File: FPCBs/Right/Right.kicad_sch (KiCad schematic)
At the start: 23 parts, among them J1 PCB, J4 shutter+1st_dial, J5 2nd Focus+Shutter, J6 FPC Focus/Shutter, SW1 Mode Dial, SW2 ON/OFF, SW3 Focus+Shutter 1, SW4 Focus+Shutter 2, U1 SG-105, U2 SG-105

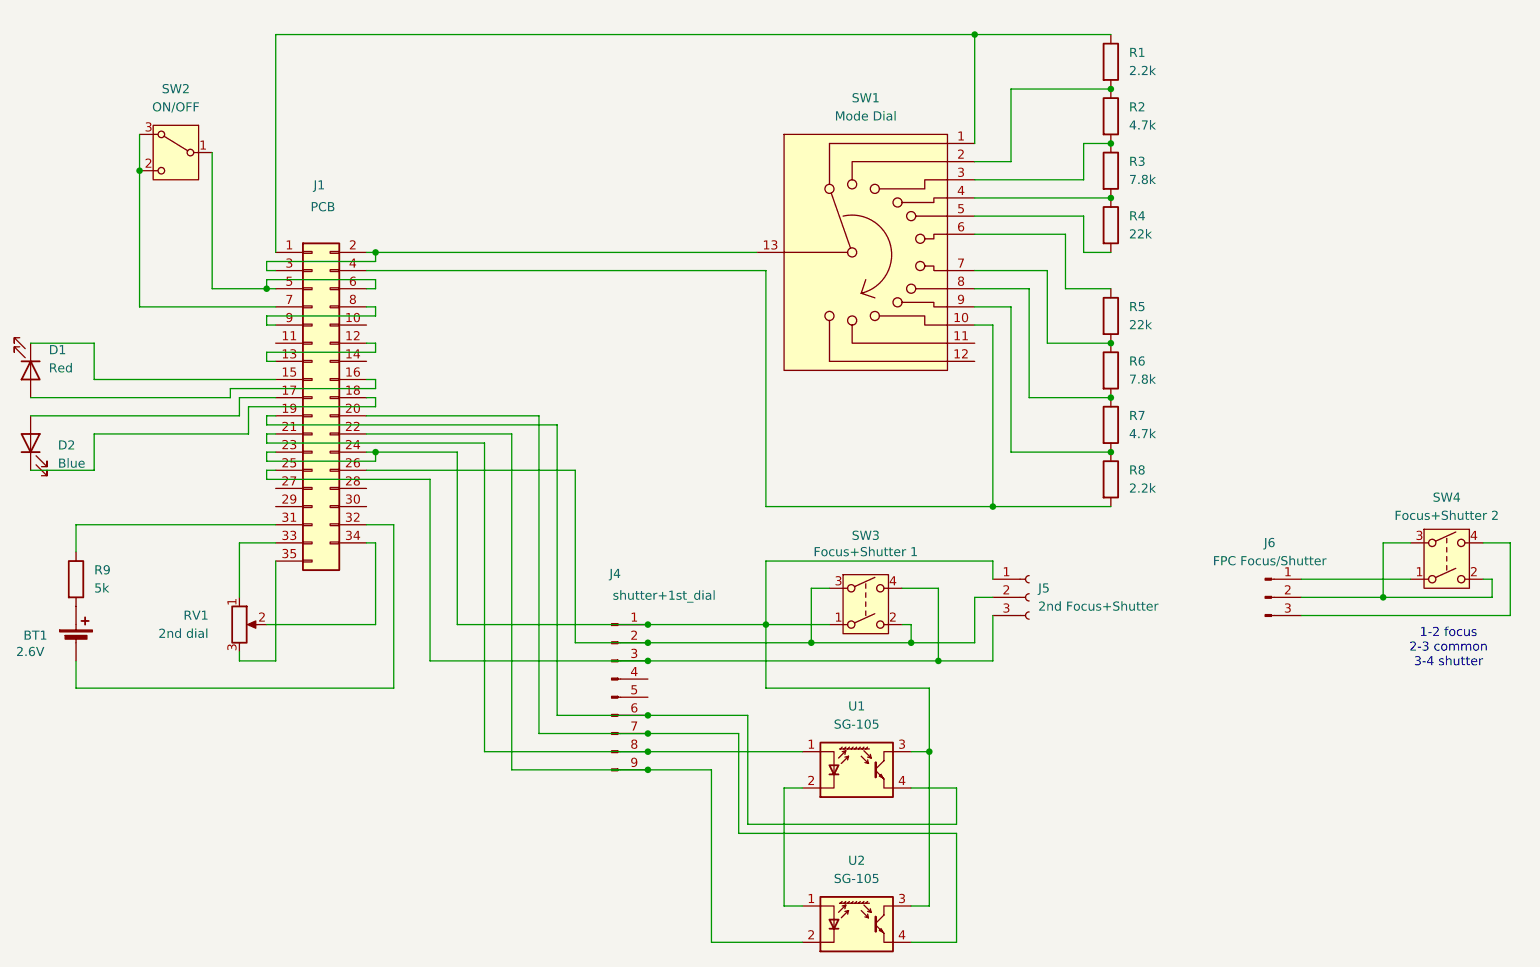
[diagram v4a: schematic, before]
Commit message: Add 1st dial connector
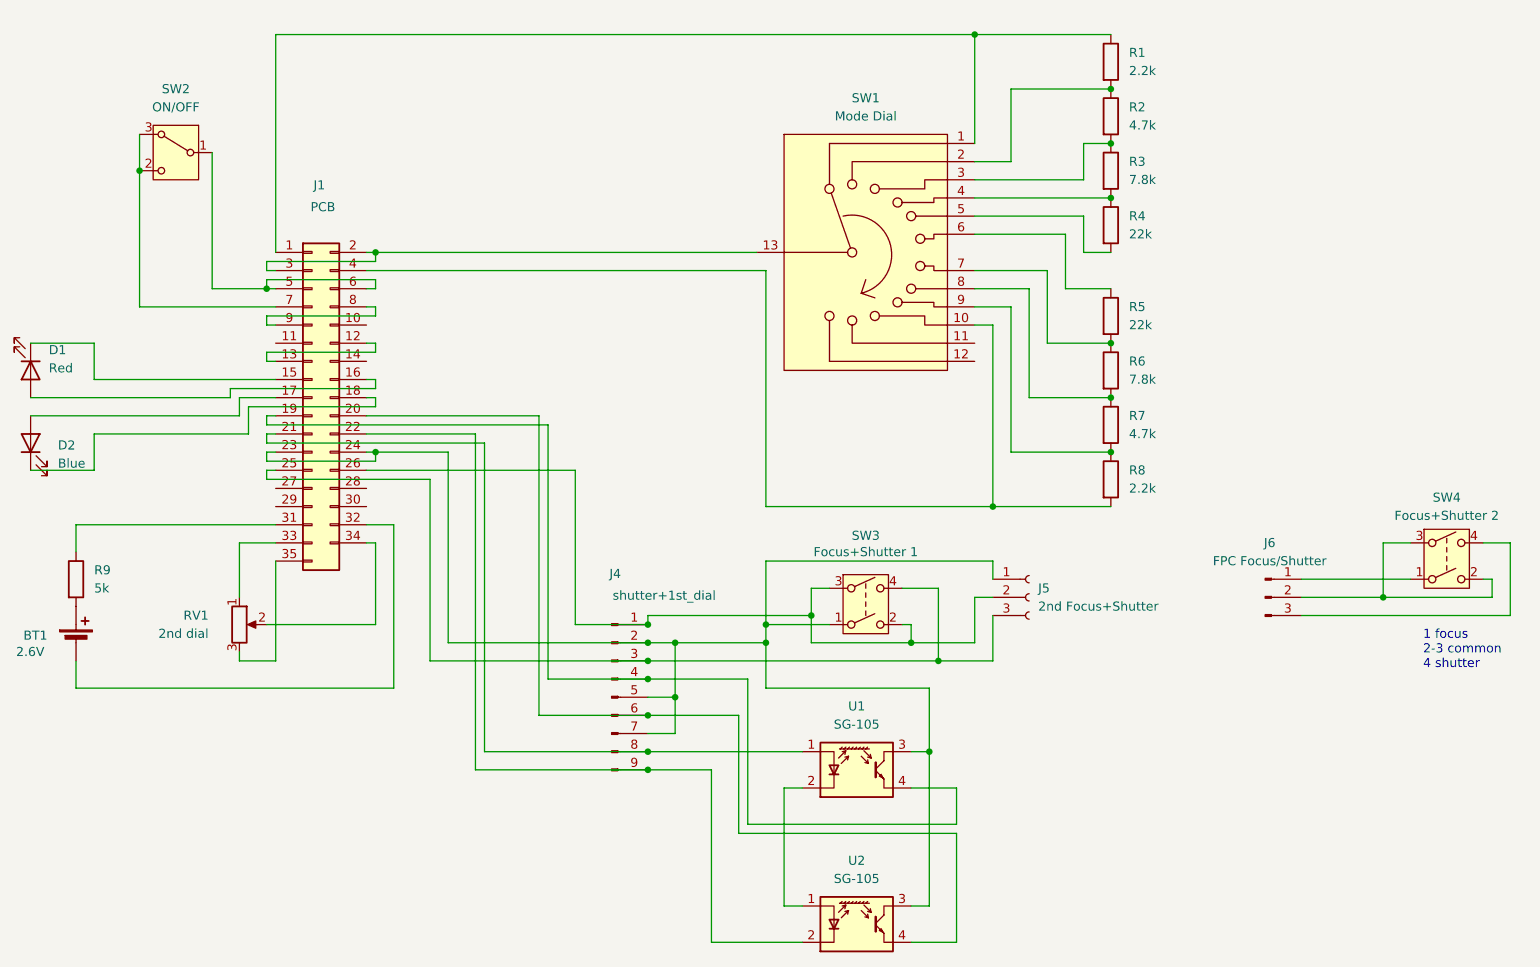
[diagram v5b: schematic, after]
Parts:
- J4: footprint (none) -> Leica-G9ii:Connector-2Rows-9Pins-0.60mm
- R1, R2, R3, R4, R5, R6, R7, R8: footprint Leica-G9ii:R_2x1mm -> Leica-G9ii:R_0603
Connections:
- net at J1.19 (Pin_19), U1.4 (E): now also J4.4 (Pin_4); no longer J4.6 (Pin_6)
- net at J1.20 (Pin_20), U2.4 (E): now also J4.6 (Pin_6); no longer J4.7 (Pin_7)
- net at J1.23 (Pin_23), J1.24 (Pin_24), J5.1 (Pin_1)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: now also J4.2 (Pin_2), J4.5 (Pin_5), J4.7 (Pin_7); no longer J4.1 (Pin_1)
- net at J1.26 (Pin_26), J5.2 (Pin_2), SW3.2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: now also J4.1 (Pin_1); no longer J4.2 (Pin_2)
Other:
- note added: "1 focus 2-3 common 4 shutter"
- note removed: "1-2 focus 2-3 common 3-4 shutter"
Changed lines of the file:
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@@
 	(generator_version "9.0")
 	(paper "A4")
-	(text "1-2 focus\n2-3 common\n3-4 shutter"
+	(text "1 focus\n2-3 common\n4 shutter"
 		(exclude_from_sim no)
-		(at 244.094 112.522 0)
+		(at 240.538 112.776 0)
 		(effects
 			(font
 				(size 1.27 1.27)
 			)
+			(justify left)
 		)
 	)
@@
 	)
 	(junction
-		(at 132.08 111.76)
-		(diameter 0)
-		(color 0 0 0 0)
-	)
-	(junction
 		(at 196.85 69.85)
 		(diameter 0)
@@
 	)
 	(junction
+		(at 132.08 109.22)
+		(diameter 0)
+		(color 0 0 0 0)
+	)
+	(junction
 		(at 60.96 45.72)
 		(diameter 0)
@@
 	)
 	(junction
-		(at 196.85 77.47)
+		(at 135.89 119.38)
 		(diameter 0)
 		(color 0 0 0 0)
 	)
 	(junction
-		(at 132.08 127)
+		(at 196.85 77.47)
 		(diameter 0)
 		(color 0 0 0 0)
 	)
 	(junction
-		(at 132.08 109.22)
+		(at 132.08 127)
 		(diameter 0)
 		(color 0 0 0 0)
@@
 	)
 	(junction
-		(at 148.59 109.22)
+		(at 180.34 92.71)
 		(diameter 0)
 		(color 0 0 0 0)
 	)
 	(junction
-		(at 180.34 92.71)
+		(at 154.94 107.95)
 		(diameter 0)
 		(color 0 0 0 0)
 	)
 	(junction
-		(at 132.08 121.92)
+		(at 148.59 109.22)
 		(diameter 0)
 		(color 0 0 0 0)
 	)
 	(junction
-		(at 154.94 111.76)
+		(at 132.08 111.76)
 		(diameter 0)
 		(color 0 0 0 0)
@@
 	)
 	(junction
+		(at 132.08 116.84)
+		(diameter 0)
+		(color 0 0 0 0)
+	)
+	(junction
+		(at 135.89 111.76)
+		(diameter 0)
+		(color 0 0 0 0)
+	)
+	(junction
 		(at 172.72 114.3)
 		(diameter 0)
@@
 	)
 	(junction
-		(at 132.08 124.46)
+		(at 148.59 111.76)
 		(diameter 0)
 		(color 0 0 0 0)
@@
 		(color 0 0 0 0)
 	)
+	(junction
+		(at 132.08 121.92)
+		(diameter 0)
+		(color 0 0 0 0)
+	)
 	(wire
 		(pts
@@
 	(wire
 		(pts
+			(xy 132.08 107.95) (xy 132.08 109.22)
+		)
+		(stroke
+			(width 0)
+			(type default)
+		)
+	)
+	(wire
+		(pts
 			(xy 78.74 72.39) (xy 80.01 72.39)
 		)
@@
 	(wire
 		(pts
-			(xy 146.05 137.16) (xy 146.05 121.92)
+			(xy 146.05 137.16) (xy 146.05 116.84)
 		)
 		(stroke
@@
 	(wire
 		(pts
-			(xy 105.41 85.09) (xy 105.41 109.22)
+			(xy 104.14 85.09) (xy 104.14 111.76)
 		)
 		(stroke
@@
 	(wire
 		(pts
-			(xy 119.38 121.92) (xy 132.08 121.92)
+			(xy 118.11 116.84) (xy 132.08 116.84)
 		)
 		(stroke
@@
 	(wire
 		(pts
-			(xy 92.71 82.55) (xy 113.03 82.55)
+			(xy 92.71 82.55) (xy 107.95 82.55)
 		)
 		(stroke
@@
 	(wire
 		(pts
-			(xy 132.08 121.92) (xy 146.05 121.92)
+			(xy 132.08 116.84) (xy 146.05 116.84)
 		)
 		(stroke
@@
 	(wire
 		(pts
-			(xy 121.92 87.63) (xy 121.92 111.76)
+			(xy 121.92 87.63) (xy 121.92 109.22)
 		)
 		(stroke
@@
 	(wire
 		(pts
-			(xy 105.41 109.22) (xy 132.08 109.22)
+			(xy 135.89 124.46) (xy 132.08 124.46)
+		)
+		(stroke
+			(width 0)
+			(type default)
+		)
+	)
+	(wire
+		(pts
+			(xy 104.14 111.76) (xy 132.08 111.76)
 		)
 		(stroke
@@
 	(wire
 		(pts
-			(xy 113.03 82.55) (xy 113.03 129.54)
+			(xy 107.95 82.55) (xy 107.95 129.54)
 		)
 		(stroke
@@
 	(wire
 		(pts
+			(xy 148.59 100.33) (xy 148.59 109.22)
+		)
+		(stroke
+			(width 0)
+			(type default)
+		)
+	)
+	(wire
+		(pts
 			(xy 177.8 54.61) (xy 190.5 54.61)
 		)
@@
 	(wire
 		(pts
-			(xy 148.59 118.11) (xy 148.59 109.22)
+			(xy 148.59 118.11) (xy 148.59 111.76)
 		)
 		(stroke
@@
 	(wire
 		(pts
-			(xy 116.84 124.46) (xy 132.08 124.46)
+			(xy 154.94 104.14) (xy 154.94 107.95)
+		)
+		(stroke
+			(width 0)
+			(type default)
+		)
+	)
+	(wire
+		(pts
+			(xy 116.84 121.92) (xy 132.08 121.92)
 		)
 		(stroke
@@
 	(wire
 		(pts
+			(xy 135.89 111.76) (xy 135.89 119.38)
+		)
+		(stroke
+			(width 0)
+			(type default)
+		)
+	)
+	(wire
+		(pts
 			(xy 171.45 127) (xy 171.45 148.59)
 		)
@@
 	(wire
 		(pts
-			(xy 93.98 109.22) (xy 93.98 97.79)
+			(xy 148.59 109.22) (xy 148.59 111.76)
 		)
 		(stroke
@@
 	(wire
 		(pts
-			(xy 154.94 104.14) (xy 154.94 111.76)
+			(xy 93.98 109.22) (xy 93.98 97.79)
 		)
 		(stroke
@@
 	(wire
 		(pts
-			(xy 78.74 81.28) (xy 119.38 81.28)
+			(xy 78.74 81.28) (xy 118.11 81.28)
 		)
 		(stroke
@@
 	(wire
 		(pts
-			(xy 121.92 111.76) (xy 132.08 111.76)
-		)
-		(stroke
-			(width 0)
-			(type default)
-		)
-	)
-	(wire
-		(pts
 			(xy 74.93 105.41) (xy 74.93 97.79)
 		)
@@
 	(wire
 		(pts
-			(xy 93.98 85.09) (xy 105.41 85.09)
+			(xy 93.98 85.09) (xy 104.14 85.09)
 		)
 		(stroke
@@
 	(wire
 		(pts
-			(xy 132.08 109.22) (xy 148.59 109.22)
+			(xy 132.08 111.76) (xy 135.89 111.76)
 		)
 		(stroke
@@
 	(wire
 		(pts
-			(xy 132.08 111.76) (xy 154.94 111.76)
+			(xy 121.92 109.22) (xy 132.08 109.22)
 		)
 		(stroke
@@
 	(wire
 		(pts
-			(xy 116.84 80.01) (xy 116.84 124.46)
+			(xy 116.84 80.01) (xy 116.84 121.92)
 		)
 		(stroke
@@
 	(wire
 		(pts
-			(xy 113.03 129.54) (xy 132.08 129.54)
+			(xy 107.95 129.54) (xy 132.08 129.54)
 		)
 		(stroke
@@
 	(wire
 		(pts
-			(xy 148.59 100.33) (xy 148.59 109.22)
+			(xy 154.94 107.95) (xy 154.94 111.76)
 		)
 		(stroke
@@
 	(wire
 		(pts
+			(xy 135.89 119.38) (xy 135.89 124.46)
+		)
+		(stroke
+			(width 0)
+			(type default)
+		)
+	)
+	(wire
+		(pts
+			(xy 135.89 111.76) (xy 148.59 111.76)
+		)
+		(stroke
+			(width 0)
+			(type default)
+		)
+	)
+	(wire
+		(pts
 			(xy 52.07 95.25) (xy 52.07 99.06)
 		)
@@
 	(wire
 		(pts
-			(xy 144.78 124.46) (xy 144.78 138.43)
+			(xy 144.78 121.92) (xy 144.78 138.43)
 		)
 		(stroke
@@
 	(wire
 		(pts
+			(xy 135.89 119.38) (xy 132.08 119.38)
+		)
+		(stroke
+			(width 0)
+			(type default)
+		)
+	)
+	(wire
+		(pts
 			(xy 172.72 114.3) (xy 180.34 114.3)
 		)
@@
 	(wire
 		(pts
-			(xy 119.38 81.28) (xy 119.38 121.92)
+			(xy 118.11 81.28) (xy 118.11 116.84)
 		)
 		(stroke
@@
 	(wire
 		(pts
+			(xy 132.08 107.95) (xy 154.94 107.95)
+		)
+		(stroke
+			(width 0)
+			(type default)
+		)
+	)
+	(wire
+		(pts
 			(xy 172.72 104.14) (xy 172.72 114.3)
 		)
@@
 	(wire
 		(pts
-			(xy 132.08 124.46) (xy 144.78 124.46)
+			(xy 132.08 121.92) (xy 144.78 121.92)
 		)
 		(stroke
@@
 			)
 		)
-		(property "Footprint" "Leica-G9ii:R_2x1mm"
+		(property "Footprint" "Leica-G9ii:R_0603"
 			(at 195.072 88.9 90)
 			(effects
@@
 			)
 		)
-		(property "Footprint" ""
+		(property "Footprint" "Leica-G9ii:Connector-2Rows-9Pins-0.60mm"
 			(at 127 119.38 0)
 			(effects
@@
 			)
 		)
-		(property "Footprint" "Leica-G9ii:R_2x1mm"
+		(property "Footprint" "Leica-G9ii:R_0603"
 			(at 195.072 53.34 90)
 			(effects
@@
 			)
 		)
-		(property "Footprint" "Leica-G9ii:R_2x1mm"
+		(property "Footprint" "Leica-G9ii:R_0603"
 			(at 195.072 73.66 90)
 			(effects
@@
 			)
 		)
-		(property "Footprint" "Leica-G9ii:R_2x1mm"
+		(property "Footprint" "Leica-G9ii:R_0603"
 			(at 195.072 45.72 90)
 			(effects
@@
 			)
 		)
-		(property "Footprint" "Leica-G9ii:R_2x1mm"
+		(property "Footprint" "Leica-G9ii:R_0603"
 			(at 195.072 81.28 90)
 			(effects
@@
 			)
 		)
-		(property "Footprint" "Leica-G9ii:R_2x1mm"
+		(property "Footprint" "Leica-G9ii:R_0603"
 			(at 195.072 30.48 90)
 			(effects
@@
 			)
 		)
-		(property "Footprint" "Leica-G9ii:R_2x1mm"
+		(property "Footprint" "Leica-G9ii:R_0603"
 			(at 195.072 66.04 90)
 			(effects
@@
 			)
 		)
-		(property "Footprint" "Leica-G9ii:R_2x1mm"
+		(property "Footprint" "Leica-G9ii:R_0603"
 			(at 195.072 38.1 90)
 			(effects

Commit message: Generate Gerbers
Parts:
- R9: footprint Leica-G9ii:R_2x1mm -> Leica-G9ii:R_0603
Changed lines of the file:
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@@
 			)
 		)
-		(property "Footprint" "Leica-G9ii:R_2x1mm"
+		(property "Footprint" "Leica-G9ii:R_0603"
 			(at 50.292 102.87 90)
 			(effects

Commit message: Update image
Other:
- note added: "A"
- note added: "C1"
- note added: "C2"
- note added: "C3"
- note added: "M"
- note added: "Movie"
- note added: "P"
- note added: "S"
- note added: "S&Q"
- note added: "iA"
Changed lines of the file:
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@@
+		)
+	)
+	(text "C1"
+		(exclude_from_sim no)
+		(at 194.056 32.766 0)
+		(effects
+			(font
+				(size 1.27 1.27)
+			)
+		)
+	)
+	(text "A"
+		(exclude_from_sim no)
+		(at 194.31 68.834 0)
+		(effects
+			(font
+				(size 1.27 1.27)
+			)
+		)
+	)
+	(text "iA"
+		(exclude_from_sim no)
+		(at 194.056 84.074 0)
+		(effects
+			(font
+				(size 1.27 1.27)
+			)
+		)
+	)
+	(text "M"
+		(exclude_from_sim no)
+		(at 194.564 58.928 0)
+		(effects
+			(font
+				(size 1.27 1.27)
+			)
+		)
+	)
+	(text "C3"
+		(exclude_from_sim no)
+		(at 194.056 91.44 0)
+		(effects
+			(font
+				(size 1.27 1.27)
+			)
+		)
+	)
+	(text "S&Q"
+		(exclude_from_sim no)
+		(at 193.04 40.64 0)
+		(effects
+			(font
+				(size 1.27 1.27)
+			)
+		)
+	)
+	(text "Movie"
+		(exclude_from_sim no)
+		(at 192.532 48.768 0)
+		(effects
+			(font
+				(size 1.27 1.27)
+			)
+		)
+	)
+	(text "S"
+		(exclude_from_sim no)
+		(at 194.564 61.468 0)
+		(effects
+			(font
+				(size 1.27 1.27)
+			)
+		)
+	)
+	(text "C2"
+		(exclude_from_sim no)
+		(at 194.056 25.4 0)
+		(effects
+			(font
+				(size 1.27 1.27)
+			)
+		)
+	)
+	(text "P"
+		(exclude_from_sim no)
+		(at 194.31 76.2 0)
+		(effects
+			(font
+				(size 1.27 1.27)
+			)
 		)
 	)

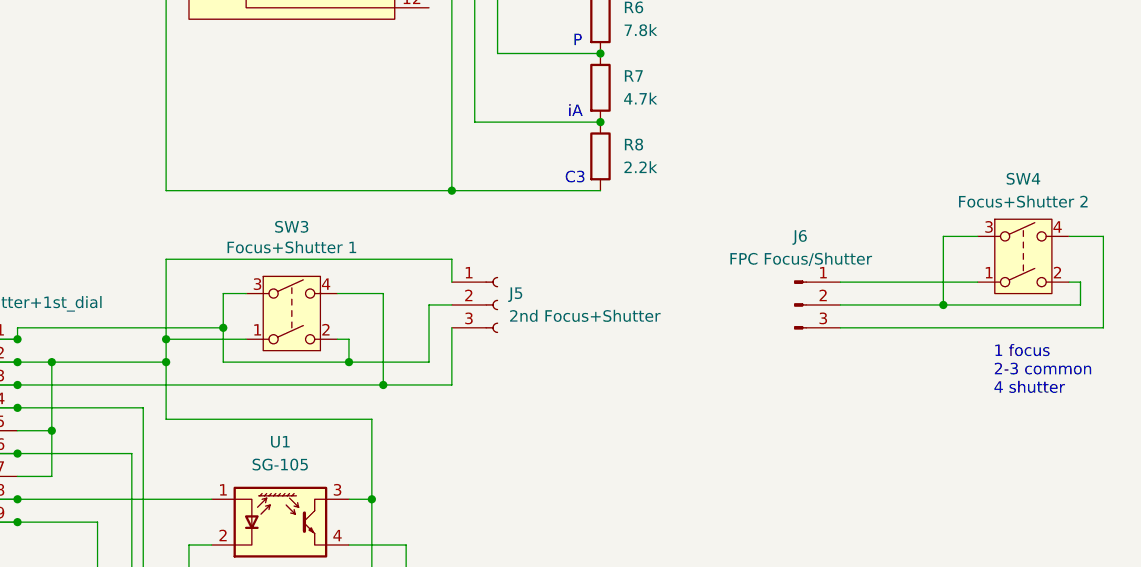
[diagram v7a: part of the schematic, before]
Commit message: Add engravings
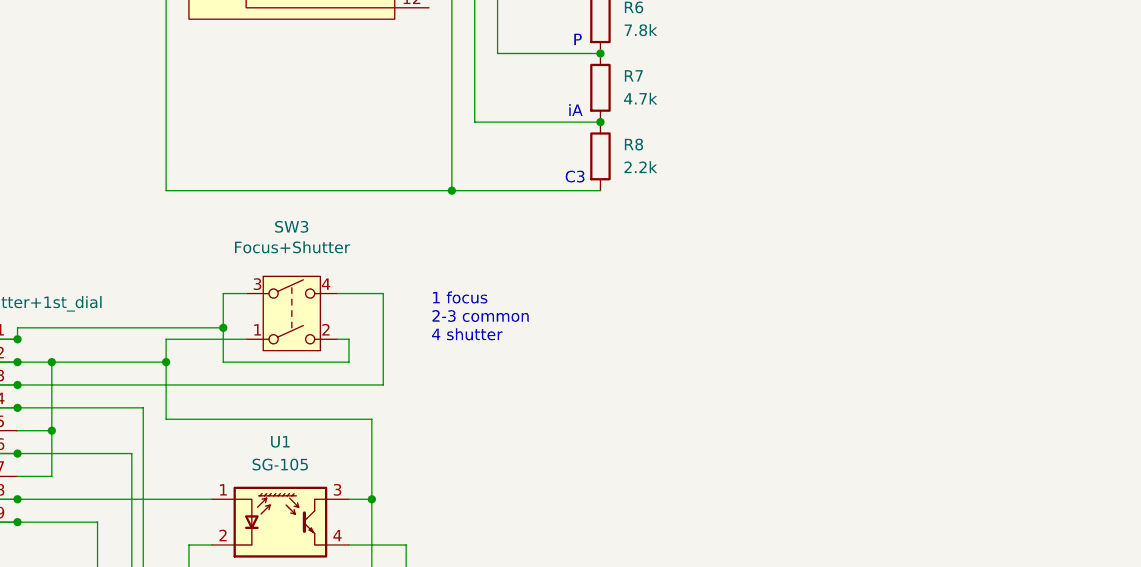
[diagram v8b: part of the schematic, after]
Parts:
- removed J5: 2nd Focus+Shutter, Leica-G9ii:Connector-Springs-3Pins, symbol Connector:Conn_01x03_Socket
- removed J6: FPC Focus/Shutter, Leica-G9ii:FPC-Springs-3Pins, symbol Connector:Conn_01x03_Pin
- removed SW4: Focus+Shutter 2, Leica-G9ii:Shutter_Olympus, symbol Switch:SW_DPST
- SW3: value Focus+Shutter 1 -> Focus+Shutter
